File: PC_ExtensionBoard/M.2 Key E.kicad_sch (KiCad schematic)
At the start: 18 parts, among them J100 Bus_M.2_2199230-2, U2 10GHz

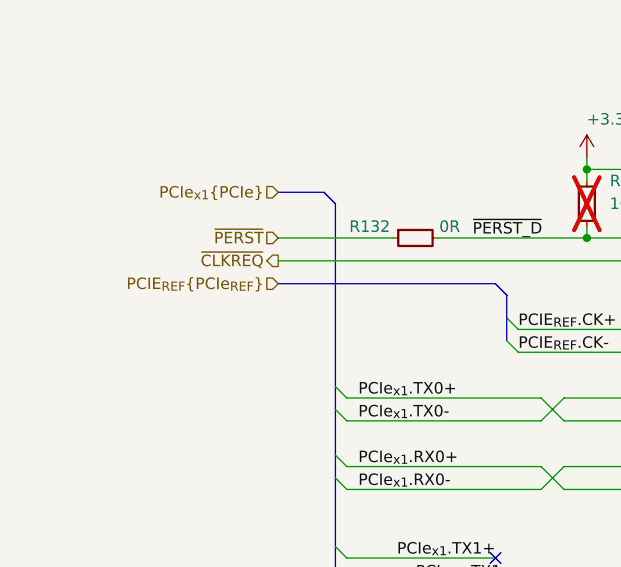
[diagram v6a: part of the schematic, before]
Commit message: update diff pair routing
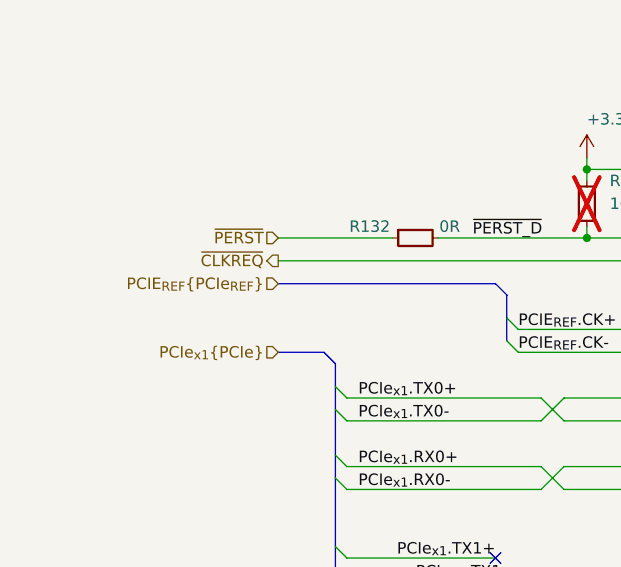
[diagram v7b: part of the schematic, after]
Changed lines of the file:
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@@
 	(bus
 		(pts
-			(xy 43.18 50.8) (xy 43.18 71.12)
+			(xy 43.18 68.58) (xy 43.18 71.12)
 		)
 		(stroke
@@
 	(bus
 		(pts
-			(xy 41.91 49.53) (xy 43.18 50.8)
+			(xy 41.91 67.31) (xy 43.18 68.58)
 		)
 		(stroke
@@
 	(bus
 		(pts
-			(xy 36.83 49.53) (xy 41.91 49.53)
+			(xy 36.83 67.31) (xy 41.91 67.31)
 		)
 		(stroke
@@
 	(hierarchical_label "PCIe_{x1}{PCIe}"
 		(shape input)
-		(at 36.83 49.53 180)
-		(effects
-			(font
+		(at 36.83 67.31 180)
+		(effects
+			(font

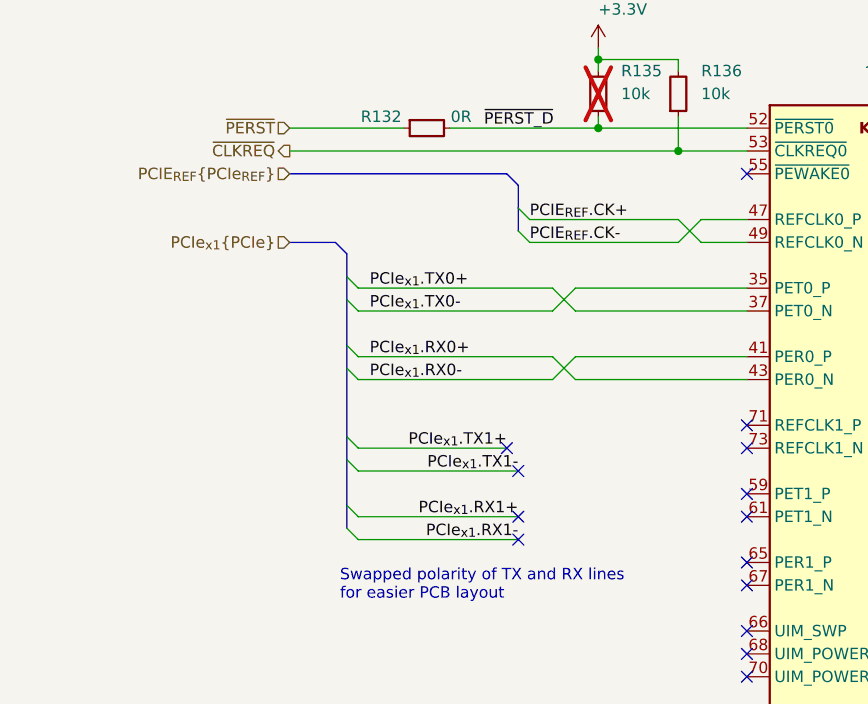
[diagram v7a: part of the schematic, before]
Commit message: attempts with impedance control
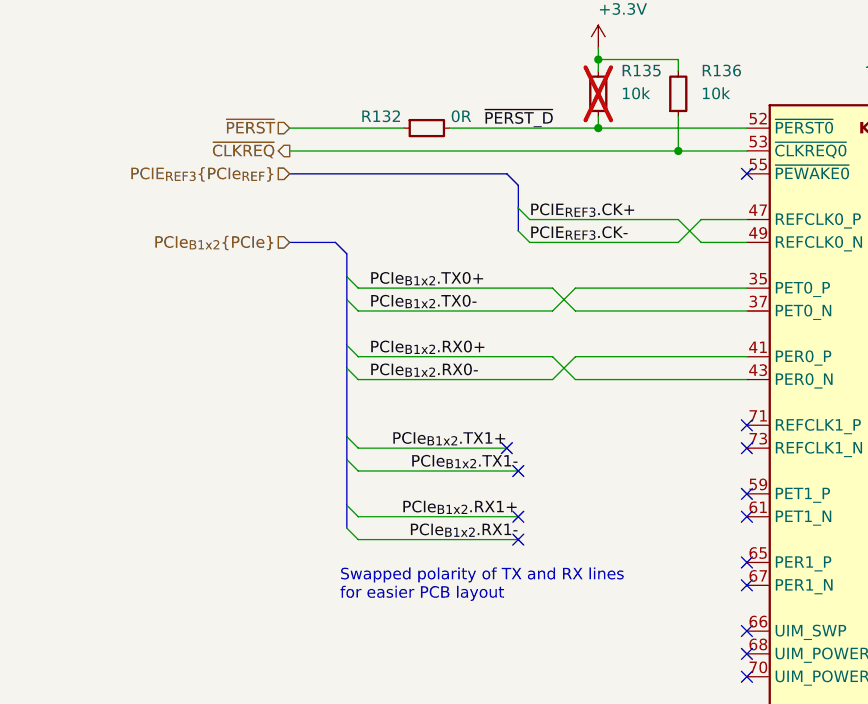
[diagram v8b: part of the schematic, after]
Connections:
- net PCIE_{REF}.CK+ renamed PCIE_{REF3}.CK+
- net PCIE_{REF}.CK- renamed PCIE_{REF3}.CK-
- net PCIe_{x1}.RX0+ renamed PCIe_{B1x2}.RX0+
- net PCIe_{x1}.RX0- renamed PCIe_{B1x2}.RX0-
- net PCIe_{x1}.TX0+ renamed PCIe_{B1x2}.TX0+
- net PCIe_{x1}.TX0- renamed PCIe_{B1x2}.TX0-
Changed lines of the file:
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@@
 		)
 	)
-	(label "PCIe_{x1}.RX1-"
+	(label "PCIe_{B1x2}.RX1-"
 		(at 62.23 100.33 180)
 		(effects
@@
 		)
 	)
-	(label "PCIe_{x1}.RX0+"
+	(label "PCIe_{B1x2}.RX0+"
 		(at 45.72 80.01 0)
 		(effects
@@
 		)
 	)
-	(label "PCIe_{x1}.TX0+"
+	(label "PCIe_{B1x2}.TX0+"
 		(at 45.72 72.39 0)
 		(effects
@@
 		)
 	)
-	(label "PCIE_{REF}.CK+"
+	(label "PCIE_{REF3}.CK+"
 		(at 63.5 64.77 0)
 		(effects
@@
 		)
 	)
-	(label "PCIe_{x1}.RX1+"
+	(label "PCIe_{B1x2}.RX1+"
 		(at 62.23 97.79 180)
 		(effects
@@
 		)
 	)
-	(label "PCIe_{x1}.TX1+"
+	(label "PCIe_{B1x2}.TX1+"
 		(at 60.96 90.17 180)
 		(effects
@@
 		)
 	)
-	(label "PCIe_{x1}.RX0-"
+	(label "PCIe_{B1x2}.RX0-"
 		(at 45.72 82.55 0)
 		(effects
@@
 		)
 	)
-	(label "PCIE_{REF}.CK-"
+	(label "PCIE_{REF3}.CK-"
 		(at 63.5 67.31 0)
 		(effects
@@
 		)
 	)
-	(label "PCIe_{x1}.TX0-"
+	(label "PCIe_{B1x2}.TX0-"
 		(at 45.72 74.93 0)
 		(effects
@@
 		)
 	)
-	(label "PCIe_{x1}.TX1-"
+	(label "PCIe_{B1x2}.TX1-"
 		(at 62.23 92.71 180)
 		(effects
@@
 		)
 	)
-	(hierarchical_label "PCIE_{REF}{PCIe_{REF}}"
+	(hierarchical_label "PCIE_{REF3}{PCIe_{REF}}"
 		(shape input)
 		(at 36.83 59.69 180)
@@
 		)
 	)
-	(hierarchical_label "PCIe_{x1}{PCIe}"
+	(hierarchical_label "PCIe_{B1x2}{PCIe}"
 		(shape input)
 		(at 36.83 67.31 180)
